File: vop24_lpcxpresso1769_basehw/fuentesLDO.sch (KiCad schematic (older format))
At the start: 13 parts

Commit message: Esquematico: agregados hojas separadas de entradas analogicas terminadas y ads1292 sin terminar
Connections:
- net labels added: GND_BAT
- wire segments 27 -> 31
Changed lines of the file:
@@
 $Descr A4 11693 8268
 encoding utf-8
-Sheet 2 2
+Sheet 2 4
 Title ""
 Date ""
@@
 Connection ~ 7350 2600
 Connection ~ 7350 3250
+Text HLabel 4700 5000 2    60   Input ~ 0
+VBAT
+Text HLabel 4700 5200 2    60   Input ~ 0
+GND_BAT
+Wire Wire Line
+	4700 5000 4500 5000
+Wire Wire Line
+	4500 5000 4500 3850
+Connection ~ 4500 3850
+Wire Wire Line
+	4450 5200 4700 5200
+Wire Wire Line
+	4450 5200 4450 4450
+Connection ~ 4450 4450
 $EndSCHEMATC

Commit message: Esquematico Comunicacion: falta agregar USB, BLE y UART
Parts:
- 1k, R? (x2): symbol R_Small -> Device:R_Small
- C? (x4): symbol C_Small -> Device:C_Small
- D? (x2): symbol LED_Small -> Device:LED_Small
- J?: symbol Conn_01x02 -> Connector_Generic:Conn_01x02
- U? (x2): symbol MCP1700T-3302E_TT -> vop24_lpcxpresso1769_basehw-rescue:MCP1700T-3302E_TT
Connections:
- wire segments 31 -> 49

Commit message: Primera versión esquematico sin revisar
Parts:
- removed J?: Conn_01x02, symbol Connector_Generic:Conn_01x02
- added C23, C27, C28: 10uF, symbol Device:C
- added C24: 0.1uF, symbol Device:C
- added J8: Conn_01x03_Male, symbol Connector:Conn_01x03_Male
- added L1: 2.2uH, symbol Device:L
- added R28: R, symbol Device:R
- added U10: TPS63001, symbol cargaBateriaUSB:TPS63001
- gave numbers to parts that had none: 10
- renumbered 1k to 1k1, 1k to 1k2
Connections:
- net labels added: DVCC_LDO, DVCC_UD, GND_NREG, VCC_NREG
- net labels removed: GND_BAT
- wire segments 49 -> 93
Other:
- moved on the sheet: 1k1, 1k2, C21, C22, C25, C26, D1, D2, R26, R27, U8, U9

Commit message: Algunas correcciones sobre el esquemático. Falta terminar de revisar algunos conflictos del DRC
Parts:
- renumbered 1k1 to 1k101, 1k2 to 1k102, C21 to C101, C22 to C102, C23 to C103, C24 to C104, C25 to C105, C26 to C106, C27 to C107, C28 to C108, D1 to D101, D2 to D102, J8 to J101, L1 to L101, R26 to R101, R27 to R102, R28 to R103, U8 to U101, U9 to U102, U10 to U103
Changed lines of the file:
@@
 P 4400 3500
 AR Path="/5B3830F9" Ref="U?"  Part="1"
-AR Path="/5B3826CA/5B3830F9" Ref="U9"  Part="1"
-F 0 "U9" H 4400 3700 60  0000 C CNN
+AR Path="/5B3826CA/5B3830F9" Ref="U102"  Part="1"
+F 0 "U102" H 4400 3700 60  0000 C CNN
 F 1 "MCP1700T-3302E_TT" H 4400 3800 60  0000 C CNN
 F 2 "digikey-footprints:SOT-23-3" H 4600 3700 60  0001 L CNN
@@
 P 4350 4750
 AR Path="/5B383109" Ref="U?"  Part="1"
-AR Path="/5B3826CA/5B383109" Ref="U8"  Part="1"
-F 0 "U8" H 4350 4950 60  0000 C CNN
+AR Path="/5B3826CA/5B383109" Ref="U101"  Part="1"
+F 0 "U101" H 4350 4950 60  0000 C CNN
 F 1 "MCP1700T-3302E_TT" H 4350 5050 60  0000 C CNN
 F 2 "digikey-footprints:SOT-23-3" H 4550 4950 60  0001 L CNN
@@
 $EndComp
 $Comp
-L Device:C_Small C21
+L Device:C_Small C101
 U 1 1 5B383117
 P 3500 3750
-F 0 "C21" H 3510 3820 50  0000 L CNN
+F 0 "C101" H 3510 3820 50  0000 L CNN
 F 1 "1uF" H 3510 3670 50  0000 L CNN
 F 2 "" H 3500 3750 50  0001 C CNN
@@
 $EndComp
 $Comp
-L Device:C_Small C25
+L Device:C_Small C105
 U 1 1 5B38311E
 P 5300 3750
-F 0 "C25" H 5310 3820 50  0000 L CNN
+F 0 "C105" H 5310 3820 50  0000 L CNN
 F 1 "1uF" H 5310 3670 50  0000 L CNN
 F 2 "" H 5300 3750 50  0001 C CNN
@@
 $EndComp
 $Comp
-L Device:C_Small C22
+L Device:C_Small C102
 U 1 1 5B383125
 P 3550 5000
-F 0 "C22" H 3560 5070 50  0000 L CNN
+F 0 "C102" H 3560 5070 50  0000 L CNN
 F 1 "1uF" H 3560 4920 50  0000 L CNN
 F 2 "" H 3550 5000 50  0001 C CNN
@@
 $EndComp
 $Comp
-L Device:C_Small C26
+L Device:C_Small C106
 U 1 1 5B38312C
 P 5300 5000
-F 0 "C26" H 5310 5070 50  0000 L CNN
+F 0 "C106" H 5310 5070 50  0000 L CNN
 F 1 "1uF" H 5310 4920 50  0000 L CNN
 F 2 "" H 5300 5000 50  0001 C CNN
@@
 $EndComp
 $Comp
-L Device:R_Small R26
+L Device:R_Small R101
 U 1 1 5B383133
 P 3250 4150
-F 0 "R26" H 3280 4170 50  0000 L CNN
+F 0 "R101" H 3280 4170 50  0000 L CNN
 F 1 "R_Small" H 3280 4110 50  0000 L CNN
 F 2 "" H 3250 4150 50  0001 C CNN
@@
 $EndComp
 $Comp
-L Device:R_Small R27
+L Device:R_Small R102
 U 1 1 5B38313A
 P 3300 5350
-F 0 "R27" H 3330 5370 50  0000 L CNN
+F 0 "R102" H 3330 5370 50  0000 L CNN
 F 1 "R_Small" H 3330 5310 50  0000 L CNN
 F 2 "" H 3300 5350 50  0001 C CNN
@@
 GNDBAT
 $Comp
-L Device:LED_Small D1
+L Device:LED_Small D101
 U 1 1 5B383147
 P 5950 3700
-F 0 "D1" H 5900 3825 50  0000 L CNN
+F 0 "D101" H 5900 3825 50  0000 L CNN
 F 1 "LED_Small" H 5775 3600 50  0000 L CNN
 F 2 "" V 5950 3700 50  0001 C CNN
@@
 $EndComp
 $Comp
-L Device:R_Small 1k1
+L Device:R_Small 1k101
 U 1 1 5B38314E
 P 5950 4000
-F 0 "1k1" H 5980 4020 50  0000 L CNN
+F 0 "1k101" H 5980 4020 50  0000 L CNN
 F 1 "R_Small" H 5980 3960 50  0000 L CNN
 F 2 "" H 5950 4000 50  0001 C CNN
@@
 $EndComp
 $Comp
-L Device:LED_Small D2
+L Device:LED_Small D102
 U 1 1 5B383155
 P 5950 4900
-F 0 "D2" H 5900 5025 50  0000 L CNN
+F 0 "D102" H 5900 5025 50  0000 L CNN
 F 1 "LED_Small" H 5775 4800 50  0000 L CNN
 F 2 "" V 5950 4900 50  0001 C CNN
@@
 $EndComp
 $Comp
-L Device:R_Small 1k2
+L Device:R_Small 1k102
 U 1 1 5B38315C
 P 5950 5200
-F 0 "1k2" H 5980 5220 50  0000 L CNN
+F 0 "1k102" H 5980 5220 50  0000 L CNN
 F 1 "R_Small" H 5980 5160 50  0000 L CNN
 F 2 "" H 5950 5200 50  0001 C CNN
@@
 	5950 4150 6900 4150
 $Comp
-L cargaBateriaUSB:TPS63001 U10
+L cargaBateriaUSB:TPS63001 U103
 U 1 1 5BBF90D3
 P 5500 2100
-F 0 "U10" H 5500 2665 50  0000 C CNN
+F 0 "U103" H 5500 2665 50  0000 C CNN
 F 1 "TPS63001" H 5500 2574 50  0000 C CNN
 F 2 "" H 5500 2000 50  0001 C CNN
@@
 $EndComp
 $Comp
-L Device:L L1
+L Device:L L101
 U 1 1 5BBF9F99
 P 5500 1400
-F 0 "L1" V 5690 1400 50  0000 C CNN
+F 0 "L101" V 5690 1400 50  0000 C CNN
 F 1 "2.2uH" V 5599 1400 50  0000 C CNN
 F 2 "" H 5500 1400 50  0001 C CNN
@@
 	6100 1900 5950 1900
 $Comp
-L Device:C C27
+L Device:C C107
 U 1 1 5BBFC32D
 P 6600 2550
-F 0 "C27" H 6715 2596 50  0000 L CNN
+F 0 "C107" H 6715 2596 50  0000 L CNN
 F 1 "10uF" H 6715 2505 50  0000 L CNN
 F 2 "" H 6638 2400 50  0001 C CNN
@@
 $EndComp
 $Comp
-L Device:C C24
+L Device:C C104
 U 1 1 5BBFC3A7
 P 4600 2750
-F 0 "C24" H 4715 2796 50  0000 L CNN
+F 0 "C104" H 4715 2796 50  0000 L CNN
 F 1 "0.1uF" H 4715 2705 50  0000 L CNN
 F 2 "" H 4638 2600 50  0001 C CNN
@@
 $EndComp
 $Comp
-L Device:C C23
+L Device:C C103
 U 1 1 5BBFC431
 P 3800 2450
-F 0 "C23" H 3915 2496 50  0000 L CNN
+F 0 "C103" H 3915 2496 50  0000 L CNN
 F 1 "10uF" H 3915 2405 50  0000 L CNN
 F 2 "" H 3838 2300 50  0001 C CNN
@@
 $EndComp
 $Comp
-L Device:C C28
+L Device:C C108
 U 1 1 5BBFC5F5
 P 7100 2550
-F 0 "C28" H 7215 2596 50  0000 L CNN
+F 0 "C108" H 7215 2596 50  0000 L CNN
 F 1 "10uF" H 7215 2505 50  0000 L CNN
 F 2 "" H 7138 2400 50  0001 C CNN
@@
 $EndComp
 $Comp
-L Device:R R28
+L Device:R R103
 U 1 1 5BBFC68E
 P 4600 2300
-F 0 "R28" H 4670 2346 50  0000 L CNN
+F 0 "R103" H 4670 2346 50  0000 L CNN
 F 1 "R" H 4670 2255 50  0000 L CNN
 F 2 "" V 4530 2300 50  0001 C CNN
@@
 DVCC_UD
 $Comp
-L Connector:Conn_01x03_Male J8
+L Connector:Conn_01x03_Male J101
 U 1 1 5BC24F14
 P 9750 3200
-F 0 "J8" H 9856 3478 50  0000 C CNN
+F 0 "J101" H 9856 3478 50  0000 C CNN
 F 1 "Conn_01x03_Male" H 9856 3387 50  0000 C CNN
 F 2 "" H 9750 3200 50  0001 C CNN

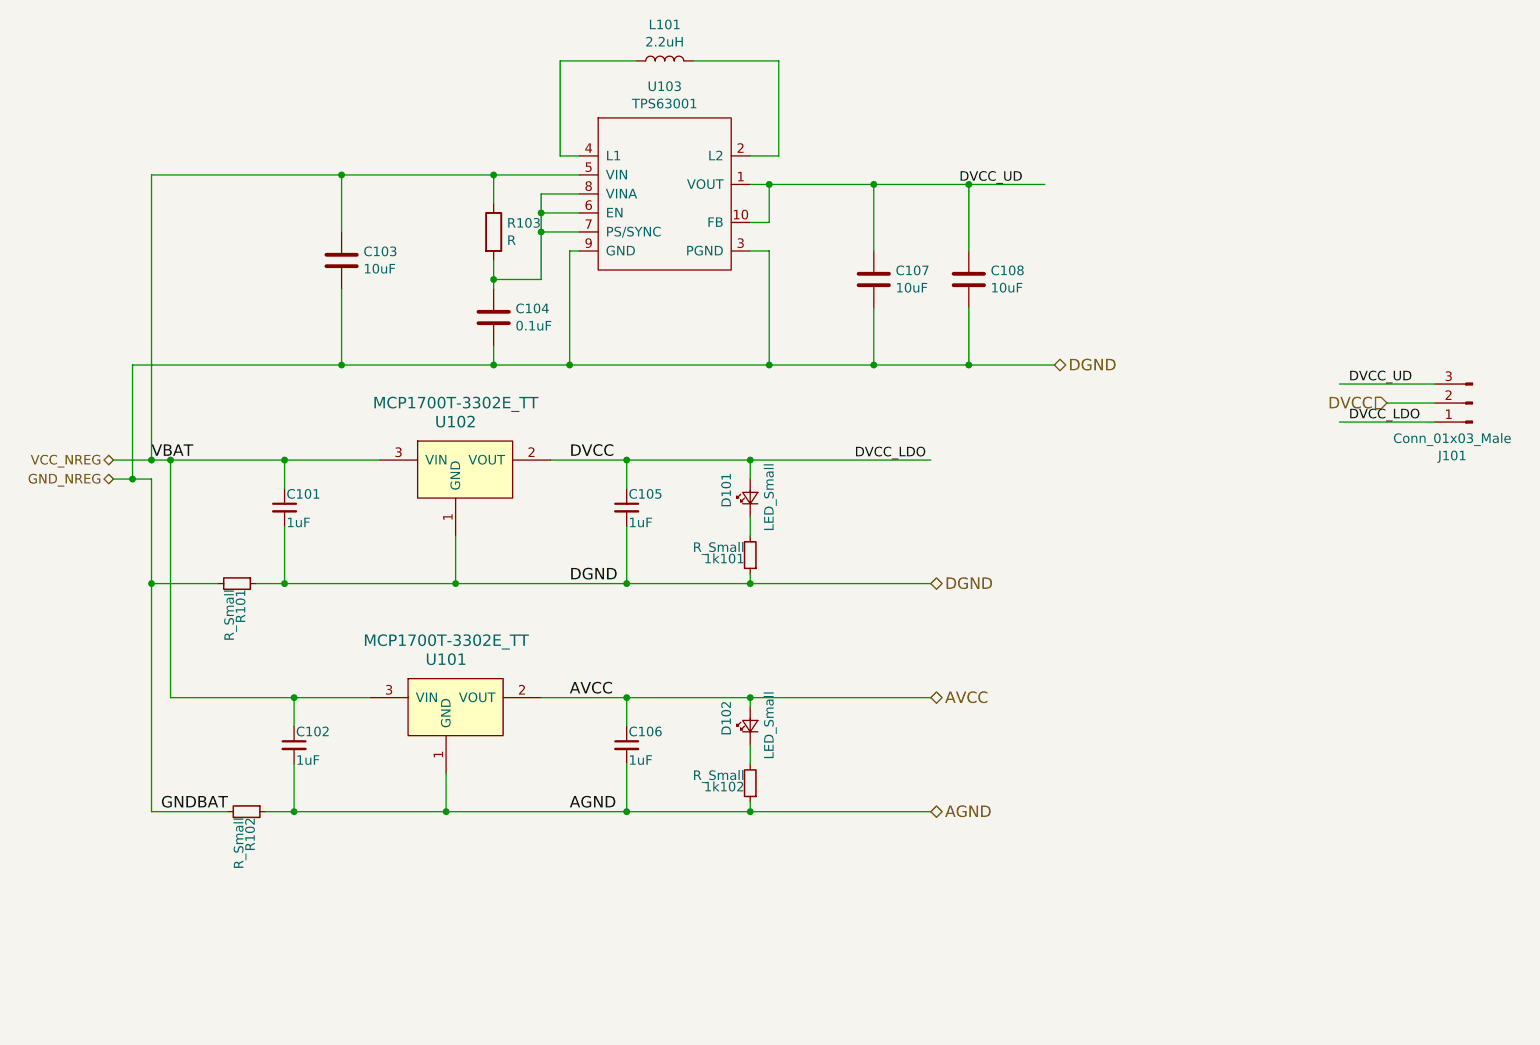
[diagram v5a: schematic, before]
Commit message: Correcciones de esquemático:    - resueltos todos los conflictos de DRC    - cambio de circutio de medicion de temp    - ordenados todas las etiquetas y valores
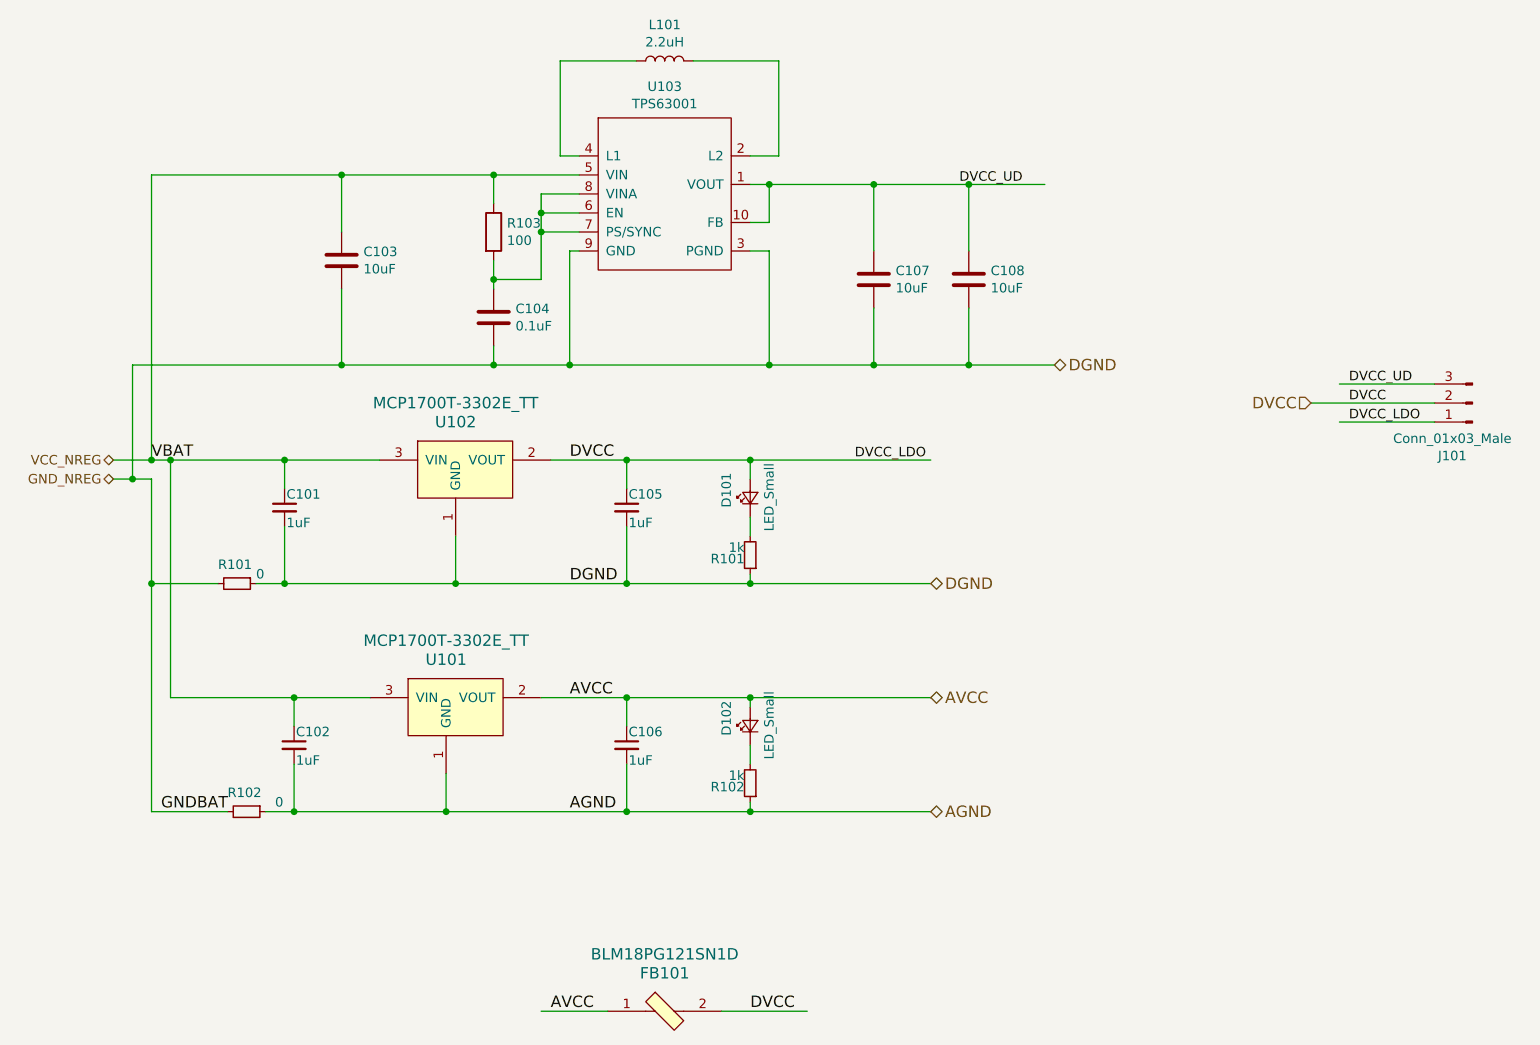
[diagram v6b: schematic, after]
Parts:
- added FB101: BLM18PG121SN1D, digikey-footprints:0603, symbol vop24_lpcxpresso1769_basehw-rescue:BLM18PG121SN1D
- R101, R102: value R_Small -> 0
- R101: renamed from 1k101; value R_Small -> 1k
- R102: renamed from 1k102; value R_Small -> 1k
- R103: value R -> 100
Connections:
- wire segments 93 -> 95
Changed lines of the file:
@@
 U 1 1 5B383133
 P 3250 4150
-F 0 "R101" H 3280 4170 50  0000 L CNN
-F 1 "R_Small" H 3280 4110 50  0000 L CNN
+F 0 "R101" V 3150 4050 50  0000 L CNN
+F 1 "0" V 3200 4250 50  0000 L CNN
 F 2 "" H 3250 4150 50  0001 C CNN
 F 3 "" H 3250 4150 50  0001 C CNN
@@
 U 1 1 5B38313A
 P 3300 5350
-F 0 "R102" H 3330 5370 50  0000 L CNN
-F 1 "R_Small" H 3330 5310 50  0000 L CNN
+F 0 "R102" V 3200 5250 50  0000 L CNN
+F 1 "0" V 3250 5500 50  0000 L CNN
 F 2 "" H 3300 5350 50  0001 C CNN
 F 3 "" H 3300 5350 50  0001 C CNN
@@
 $EndComp
 $Comp
-L Device:R_Small 1k101
+L Device:R_Small R101
 U 1 1 5B38314E
 P 5950 4000
-F 0 "1k101" H 5980 4020 50  0000 L CNN
-F 1 "R_Small" H 5980 3960 50  0000 L CNN
+F 0 "R101" H 5980 4020 50  0000 L CNN
+F 1 "1k" H 5980 3960 50  0000 L CNN
 F 2 "" H 5950 4000 50  0001 C CNN
 F 3 "" H 5950 4000 50  0001 C CNN
@@
 $EndComp
 $Comp
-L Device:R_Small 1k102
+L Device:R_Small R102
 U 1 1 5B38315C
 P 5950 5200
-F 0 "1k102" H 5980 5220 50  0000 L CNN
-F 1 "R_Small" H 5980 5160 50  0000 L CNN
+F 0 "R102" H 5980 5220 50  0000 L CNN
+F 1 "1k" H 5980 5160 50  0000 L CNN
 F 2 "" H 5950 5200 50  0001 C CNN
 F 3 "" H 5950 5200 50  0001 C CNN
@@
 Text HLabel 6900 4150 2    60   BiDi ~ 0
 DGND
-Text HLabel 9300 3200 0    60   Input ~ 0
+Text HLabel 8900 3200 0    60   Input ~ 0
 DVCC
 Connection ~ 5950 3500
@@
 P 4600 2300
 F 0 "R103" H 4670 2346 50  0000 L CNN
-F 1 "R" H 4670 2255 50  0000 L CNN
+F 1 "100" H 4670 2255 50  0000 L CNN
 F 2 "" V 4530 2300 50  0001 C CNN
 F 3 "~" H 4600 2300 50  0001 C CNN
@@
 $EndComp
 Wire Wire Line
-	9550 3200 9300 3200
-Wire Wire Line
 	9550 3300 9050 3300
 Wire Wire Line
@@
 Text HLabel 2600 3600 0    50   BiDi ~ 0
 GND_NREG
+Text Label 5950 6400 0    60   ~ 0
+DVCC
+$Comp
+L vop24_lpcxpresso1769_basehw-rescue:BLM18PG121SN1D FB?
+U 1 1 5BE5DDBC
+P 5500 6400
+AR Path="/5B3D4A05/5BE5DDBC" Ref="FB?"  Part="1"
+AR Path="/5B3826CA/5BE5DDBC" Ref="FB101"  Part="1"
+F 0 "FB101" H 5500 6600 60  0000 C CNN
+F 1 "BLM18PG121SN1D" H 5500 6700 60  0000 C CNN
+F 2 "digikey-footprints:0603" H 5700 6600 60  0001 L CNN
+F 3 "https://www.murata.com/en-us/products/productdata/8796738650142/ENFA0003.pdf" H 5700 6700 60  0001 L CNN
+F 4 "490-1037-1-ND" H 5700 6800 60  0001 L CNN "Digi-Key_PN"
+F 5 "BLM18PG121SN1D" H 5700 6900 60  0001 L CNN "MPN"
+F 6 "Filters" H 5700 7000 60  0001 L CNN "Category"
+F 7 "Ferrite Beads and Chips" H 5700 7100 60  0001 L CNN "Family"
+F 8 "https://www.murata.com/en-us/products/productdata/8796738650142/ENFA0003.pdf" H 5700 7200 60  0001 L CNN "DK_Datasheet_Link"
+F 9 "/product-detail/en/murata-electronics-north-america/BLM18PG121SN1D/490-1037-1-ND/584485" H 5700 7300 60  0001 L CNN "DK_Detail_Page"
+F 10 "FERRITE BEAD 120 OHM 0603 1LN" H 5700 7400 60  0001 L CNN "Description"
+F 11 "Murata Electronics North America" H 5700 7500 60  0001 L CNN "Manufacturer"
+F 12 "Active" H 5700 7600 60  0001 L CNN "Status"
+	1    5500 6400
+	1    0    0    -1
+$EndComp
+Wire Wire Line
+	5800 6400 6250 6400
+Wire Wire Line
+	5200 6400 4850 6400
+Text Label 4900 6400 0    60   ~ 0
+AVCC
+Text Label 9100 3200 0    50   ~ 0
+DVCC
+Wire Wire Line
+	8900 3200 9550 3200
 $EndSCHEMATC

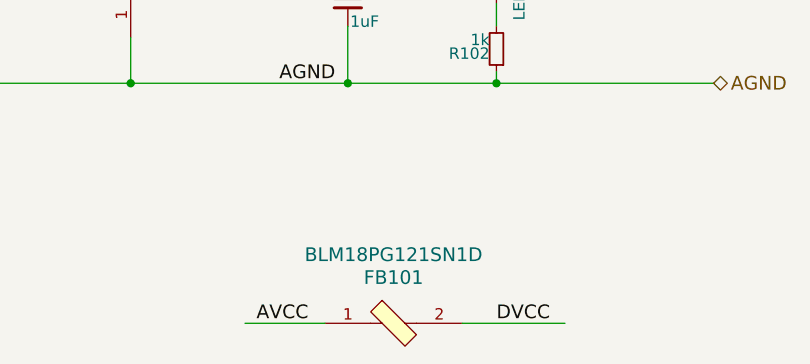
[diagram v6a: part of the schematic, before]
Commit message: Se agregaron la mayoría de los footprints de los ICs
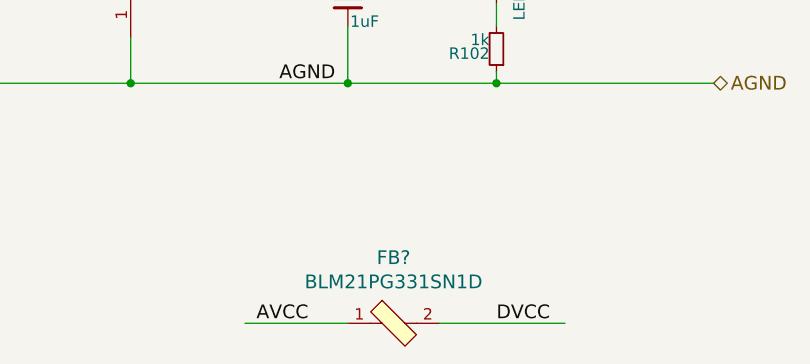
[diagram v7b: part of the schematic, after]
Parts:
- removed FB101: BLM18PG121SN1D, digikey-footprints:0603, symbol vop24_lpcxpresso1769_basehw-rescue:BLM18PG121SN1D
- added FB?: BLM21PG331SN1D, digikey-footprints:0805, symbol dk_Ferrite-Beads-and-Chips:BLM21PG331SN1D
- L101: footprint (none) -> Inductor_SMD:L_0805_2012Metric_Pad1.15x1.40mm_HandSolder
- U103: footprint (none) -> Package_SON:VSON-10-1EP_3x3mm_P0.5mm_EP1.65x2.4mm_ThermalVias
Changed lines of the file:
@@
 F 0 "U103" H 5500 2665 50  0000 C CNN
 F 1 "TPS63001" H 5500 2574 50  0000 C CNN
-F 2 "" H 5500 2000 50  0001 C CNN
+F 2 "Package_SON:VSON-10-1EP_3x3mm_P0.5mm_EP1.65x2.4mm_ThermalVias" H 5500 2000 50  0001 C CNN
 F 3 "" H 5500 2000 50  0001 C CNN
 	1    5500 2100
@@
 F 0 "L101" V 5690 1400 50  0000 C CNN
 F 1 "2.2uH" V 5599 1400 50  0000 C CNN
-F 2 "" H 5500 1400 50  0001 C CNN
+F 2 "Inductor_SMD:L_0805_2012Metric_Pad1.15x1.40mm_HandSolder" H 5500 1400 50  0001 C CNN
 F 3 "~" H 5500 1400 50  0001 C CNN
 	1    5500 1400
@@
 Text Label 5950 6400 0    60   ~ 0
 DVCC
-$Comp
-L vop24_lpcxpresso1769_basehw-rescue:BLM18PG121SN1D FB?
-U 1 1 5BE5DDBC
-P 5500 6400
-AR Path="/5B3D4A05/5BE5DDBC" Ref="FB?"  Part="1"
-AR Path="/5B3826CA/5BE5DDBC" Ref="FB101"  Part="1"
-F 0 "FB101" H 5500 6600 60  0000 C CNN
-F 1 "BLM18PG121SN1D" H 5500 6700 60  0000 C CNN
-F 2 "digikey-footprints:0603" H 5700 6600 60  0001 L CNN
-F 3 "https://www.murata.com/en-us/products/productdata/8796738650142/ENFA0003.pdf" H 5700 6700 60  0001 L CNN
-F 4 "490-1037-1-ND" H 5700 6800 60  0001 L CNN "Digi-Key_PN"
-F 5 "BLM18PG121SN1D" H 5700 6900 60  0001 L CNN "MPN"
-F 6 "Filters" H 5700 7000 60  0001 L CNN "Category"
-F 7 "Ferrite Beads and Chips" H 5700 7100 60  0001 L CNN "Family"
-F 8 "https://www.murata.com/en-us/products/productdata/8796738650142/ENFA0003.pdf" H 5700 7200 60  0001 L CNN "DK_Datasheet_Link"
-F 9 "/product-detail/en/murata-electronics-north-america/BLM18PG121SN1D/490-1037-1-ND/584485" H 5700 7300 60  0001 L CNN "DK_Detail_Page"
-F 10 "FERRITE BEAD 120 OHM 0603 1LN" H 5700 7400 60  0001 L CNN "Description"
-F 11 "Murata Electronics North America" H 5700 7500 60  0001 L CNN "Manufacturer"
-F 12 "Active" H 5700 7600 60  0001 L CNN "Status"
-	1    5500 6400
-	1    0    0    -1
-$EndComp
-Wire Wire Line
-	5800 6400 6250 6400
-Wire Wire Line
-	5200 6400 4850 6400
 Text Label 4900 6400 0    60   ~ 0
 AVCC
@@
 Wire Wire Line
 	8900 3200 9550 3200
+$Comp
+L dk_Ferrite-Beads-and-Chips:BLM21PG331SN1D FB?
+U 1 1 5BD41945
+P 5500 6400
+F 0 "FB?" H 5500 6687 60  0000 C CNN
+F 1 "BLM21PG331SN1D" H 5500 6581 60  0000 C CNN
+F 2 "digikey-footprints:0805" H 5700 6600 60  0001 L CNN
+F 3 "https://www.murata.com/en-us/products/productdata/8796738977822/ENFA0005.pdf" H 5700 6700 60  0001 L CNN
+F 4 "490-5988-1-ND" H 5700 6800 60  0001 L CNN "Digi-Key_PN"
+F 5 "BLM21PG331SN1D" H 5700 6900 60  0001 L CNN "MPN"
+F 6 "Filters" H 5700 7000 60  0001 L CNN "Category"
+F 7 "Ferrite Beads and Chips" H 5700 7100 60  0001 L CNN "Family"
+F 8 "https://www.murata.com/en-us/products/productdata/8796738977822/ENFA0005.pdf" H 5700 7200 60  0001 L CNN "DK_Datasheet_Link"
+F 9 "/product-detail/en/murata-electronics-north-america/BLM21PG331SN1D/490-5988-1-ND/3845188" H 5700 7300 60  0001 L CNN "DK_Detail_Page"
+F 10 "FERRITE BEAD 330 OHM 0805 1LN" H 5700 7400 60  0001 L CNN "Description"
+F 11 "Murata Electronics North America" H 5700 7500 60  0001 L CNN "Manufacturer"
+F 12 "Active" H 5700 7600 60  0001 L CNN "Status"
+	1    5500 6400
+	1    0    0    -1
+$EndComp
+Wire Wire Line
+	4850 6400 5300 6400
+Wire Wire Line
+	5700 6400 6250 6400
 $EndSCHEMATC
